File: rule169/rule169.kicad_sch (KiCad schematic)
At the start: 35 parts, among them U1 xiao-ble

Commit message: add project files
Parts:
- added L1, L2, L3: LED, Keyboard Footprints:LED_3mm_reversible, symbol Device:LED
- added R1, R2, R3: 220, Keyboard Footprints:R_1206_DoubleSided, symbol Device:R
- added RSW1: SW_Push, Keyboard Footprints:ResetSW, symbol Switch:SW_Push
- U1: footprint Keyboard Footprints:xiao-ble-tht -> Keyboard Footprints:xiao seed ble
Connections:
- net MCU- is gone; now on net GND: U1.20 (GND)
- net GND: now also R1.2, R2.2, R3.2, RSW1.1
- net MCU+: now also PSW1.1 (A)
- net LED0: now reaches U1.1 (A2/0.02_H)
- net LED0: now also L1.2 (A)
- net RESET: now reaches U1.17 (RESET)
- net RESET: now also RSW1.2
- net LED1: now reaches U1.2 (A4/0.03_H)
- net LED1: now also L2.2 (A)
- net LED2: now reaches U1.3 (A10/0.28)
- net LED2: now also L3.2 (A)
- new net PL1: L1.1 (K), R1.1
- new net PL2: L2.1 (K), R2.1
- new net PL3: L3.1 (K), R3.1
- no-connect marks 11 -> 8
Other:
- note added: "LED"
- note added: "RESET"
- title: (none) -> Automaton 169
- moved on the sheet: BT1, D1, D10, D11, D12, D13, D14, D15, D16, D2, D3, D4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

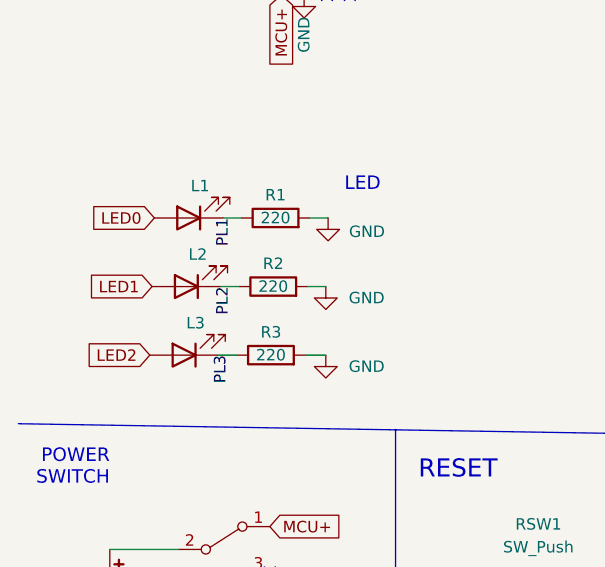
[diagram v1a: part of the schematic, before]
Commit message: add silkscreen
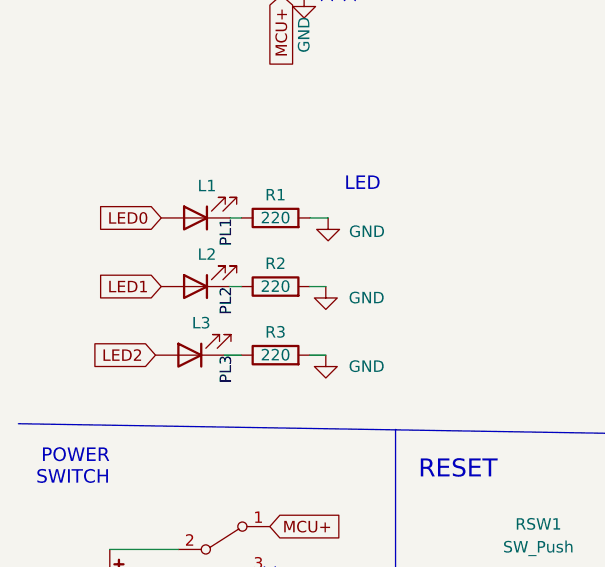
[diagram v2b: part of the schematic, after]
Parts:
- renumbered L2 to L1, L3 to L2, L1 to L3
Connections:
- net LED0: now also L1.2 (A); no longer L3.2 (A)
- net LED1: now also L2.2 (A); no longer L1.2 (A)
- net LED2: now also L3.2 (A); no longer L2.2 (A)
- net PL1: now also L1.1 (K); no longer L3.1 (K)
- net PL2: now also L2.1 (K); no longer L1.1 (K)
- net PL3: now also L3.1 (K); no longer L2.1 (K)
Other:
- moved on the sheet: L1, L2, L3, R3
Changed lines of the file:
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@@
     (stroke (width 0) (type default) (color 0 0 0 0))
   )
-  (wire (pts (xy 36.576 87.63) (xy 34.544 87.63))
+  (wire (pts (xy 35.56 87.63) (xy 36.83 87.63))
+    (stroke (width 0) (type default) (color 0 0 0 0))
+  )
+  (wire (pts (xy 35.56 80.01) (xy 36.83 80.01))
     (stroke (width 0) (type default) (color 0 0 0 0))
   )
@@
     (stroke (width 0) (type default) (color 0 0 0 0))
   )
-  (wire (pts (xy 46.228 95.25) (xy 43.942 95.25))
+  (wire (pts (xy 46.228 95.25) (xy 44.45 95.25))
     (stroke (width 0) (type default) (color 0 0 0 0))
   )
@@
     (stroke (width 0) (type default) (color 0 0 0 0))
   )
+  (wire (pts (xy 34.925 95.25) (xy 36.83 95.25))
+    (stroke (width 0) (type default) (color 0 0 0 0))
+  )
   (wire (pts (xy 142.113 26.162) (xy 142.113 32.512))
     (stroke (width 0) (type default) (color 0 0 0 0))
@@
     (stroke (width 0) (type default) (color 0 0 0 0))
   )
-  (wire (pts (xy 36.83 80.01) (xy 34.798 80.01))
-    (stroke (width 0) (type default) (color 0 0 0 0))
-  )
   (wire (pts (xy 153.035 69.596) (xy 153.035 87.376))
     (stroke (width 0) (type default) (color 0 0 0 0))
@@
     (stroke (width 0) (type default) (color 0 0 0 0))
   )
-  (wire (pts (xy 46.228 87.63) (xy 44.196 87.63))
+  (wire (pts (xy 46.228 87.63) (xy 44.45 87.63))
     (stroke (width 0) (type default) (color 0 0 0 0))
   )
@@
   )
   (wire (pts (xy 169.037 97.536) (xy 179.959 97.536))
-    (stroke (width 0) (type default) (color 0 0 0 0))
-  )
-  (wire (pts (xy 36.322 95.25) (xy 34.29 95.25))
     (stroke (width 0) (type default) (color 0 0 0 0))
   )
@@
     (effects (font (size 1.5 1.5)) (justify right bottom))
   )
-  (label "PL3" (at 35.56 95.25 270)
+  (label "PL3" (at 36.195 95.25 270)
     (effects (font (size 1.27 1.27)) (justify right bottom))
   )
-  (label "PL2" (at 35.814 87.63 270)
+  (label "PL2" (at 36.195 87.63 270)
     (effects (font (size 1.27 1.27)) (justify right bottom))
   )
-  (label "PL1" (at 35.814 80.01 270)
+  (label "PL1" (at 36.195 80.01 270)
     (effects (font (size 1.27 1.27)) (justify right bottom))
   )
@@
     )
   )
-  (global_label "LED1" (shape input) (at 26.924 87.63 180) (fields_autoplaced)
-    (effects (font (size 1.27 1.27)) (justify right))
-    (property "Intersheet References" "${INTERSHEET_REFS}" (id 0) (at 19.8542 87.5506 0)
+  (global_label "LED1" (shape input) (at 27.94 87.63 180) (fields_autoplaced)
+    (effects (font (size 1.27 1.27)) (justify right))
+    (property "Intersheet References" "${INTERSHEET_REFS}" (id 0) (at 20.8702 87.5506 0)
       (effects (font (size 1.27 1.27)) (justify right) hide)
     )
@@
     )
   )
-  (global_label "LED0" (shape input) (at 27.178 80.01 180) (fields_autoplaced)
-    (effects (font (size 1.27 1.27)) (justify right))
-    (property "Intersheet References" "${INTERSHEET_REFS}" (id 0) (at 20.1082 79.9306 0)
-      (effects (font (size 1.27 1.27)) (justify right) hide)
-    )
-  )
-  (global_label "LED2" (shape input) (at 26.67 95.25 180) (fields_autoplaced)
-    (effects (font (size 1.27 1.27)) (justify right))
-    (property "Intersheet References" "${INTERSHEET_REFS}" (id 0) (at 19.6002 95.1706 0)
+  (global_label "LED0" (shape input) (at 27.94 80.01 180) (fields_autoplaced)
+    (effects (font (size 1.27 1.27)) (justify right))
+    (property "Intersheet References" "${INTERSHEET_REFS}" (id 0) (at 20.8702 79.9306 0)
+      (effects (font (size 1.27 1.27)) (justify right) hide)
+    )
+  )
+  (global_label "LED2" (shape input) (at 27.305 95.25 180) (fields_autoplaced)
+    (effects (font (size 1.27 1.27)) (justify right))
+    (property "Intersheet References" "${INTERSHEET_REFS}" (id 0) (at 20.2352 95.1706 0)
       (effects (font (size 1.27 1.27)) (justify right) hide)
     )
@@
     (pin "2")
   )
-  (symbol (lib_id "Device:LED") (at 30.734 87.63 180) (unit 1)
-    (in_bom yes) (on_board yes)
-    (property "Reference" "L2" (id 0) (at 32.004 84.074 0))
-    (property "Value" "LED" (id 1) (at 32.3215 82.296 0)
-      (effects (font (size 1.27 1.27)) hide)
-    )
-    (property "Footprint" "Keyboard Footprints:LED_3mm_reversible" (id 2) (at 30.734 87.63 0)
-      (effects (font (size 1.27 1.27)) hide)
-    )
-    (property "Datasheet" "~" (id 3) (at 30.734 87.63 0)
+  (symbol (lib_id "Device:LED") (at 31.75 80.01 180) (unit 1)
+    (in_bom yes) (on_board yes)
+    (property "Reference" "L1" (id 0) (at 33.02 76.454 0))
+    (property "Value" "LED" (id 1) (at 33.3375 74.676 0)
+      (effects (font (size 1.27 1.27)) hide)
+    )
+    (property "Footprint" "Keyboard Footprints:LED_3mm_reversible" (id 2) (at 31.75 80.01 0)
+      (effects (font (size 1.27 1.27)) hide)
+    )
+    (property "Datasheet" "~" (id 3) (at 31.75 80.01 0)
       (effects (font (size 1.27 1.27)) hide)
     )
@@
     (pin "1")
   )
-  (symbol (lib_id "Device:R") (at 40.132 95.25 90) (unit 1)
-    (in_bom yes) (on_board yes)
-    (property "Reference" "R3" (id 0) (at 40.132 92.71 90))
-    (property "Value" "220" (id 1) (at 40.132 95.25 90))
-    (property "Footprint" "Keyboard Footprints:R_1206_DoubleSided" (id 2) (at 40.132 97.028 90)
-      (effects (font (size 1.27 1.27)) hide)
-    )
-    (property "Datasheet" "~" (id 3) (at 40.132 95.25 0)
+  (symbol (lib_id "Device:R") (at 40.64 95.25 90) (unit 1)
+    (in_bom yes) (on_board yes)
+    (property "Reference" "R3" (id 0) (at 40.64 92.71 90))
+    (property "Value" "220" (id 1) (at 40.64 95.25 90))
+    (property "Footprint" "Keyboard Footprints:R_1206_DoubleSided" (id 2) (at 40.64 97.028 90)
+      (effects (font (size 1.27 1.27)) hide)
+    )
+    (property "Datasheet" "~" (id 3) (at 40.64 95.25 0)
       (effects (font (size 1.27 1.27)) hide)
     )
@@
     (pin "1")
   )
-  (symbol (lib_id "Device:LED") (at 30.48 95.25 180) (unit 1)
-    (in_bom yes) (on_board yes)
-    (property "Reference" "L3" (id 0) (at 31.75 91.694 0))
-    (property "Value" "LED" (id 1) (at 32.0675 89.916 0)
-      (effects (font (size 1.27 1.27)) hide)
-    )
-    (property "Footprint" "Keyboard Footprints:LED_3mm_reversible" (id 2) (at 30.48 95.25 0)
-      (effects (font (size 1.27 1.27)) hide)
-    )
-    (property "Datasheet" "~" (id 3) (at 30.48 95.25 0)
+  (symbol (lib_id "Device:LED") (at 31.75 87.63 180) (unit 1)
+    (in_bom yes) (on_board yes)
+    (property "Reference" "L2" (id 0) (at 33.02 84.074 0))
+    (property "Value" "LED" (id 1) (at 33.3375 82.296 0)
+      (effects (font (size 1.27 1.27)) hide)
+    )
+    (property "Footprint" "Keyboard Footprints:LED_3mm_reversible" (id 2) (at 31.75 87.63 0)
+      (effects (font (size 1.27 1.27)) hide)
+    )
+    (property "Datasheet" "~" (id 3) (at 31.75 87.63 0)
       (effects (font (size 1.27 1.27)) hide)
     )
@@
     (pin "2")
   )
-  (symbol (lib_id "Device:R") (at 40.386 87.63 90) (unit 1)
-    (in_bom yes) (on_board yes)
-    (property "Reference" "R2" (id 0) (at 40.386 85.09 90))
-    (property "Value" "220" (id 1) (at 40.386 87.63 90))
-    (property "Footprint" "Keyboard Footprints:R_1206_DoubleSided" (id 2) (at 40.386 89.408 90)
-      (effects (font (size 1.27 1.27)) hide)
-    )
-    (property "Datasheet" "~" (id 3) (at 40.386 87.63 0)
+  (symbol (lib_id "Device:R") (at 40.64 87.63 90) (unit 1)
+    (in_bom yes) (on_board yes)
+    (property "Reference" "R2" (id 0) (at 40.64 85.09 90))
+    (property "Value" "220" (id 1) (at 40.64 87.63 90))
+    (property "Footprint" "Keyboard Footprints:R_1206_DoubleSided" (id 2) (at 40.64 89.408 90)
+      (effects (font (size 1.27 1.27)) hide)
+    )
+    (property "Datasheet" "~" (id 3) (at 40.64 87.63 0)
       (effects (font (size 1.27 1.27)) hide)
     )
@@
     (pin "2")
   )
-  (symbol (lib_id "Device:LED") (at 30.988 80.01 180) (unit 1)
-    (in_bom yes) (on_board yes)
-    (property "Reference" "L1" (id 0) (at 32.258 76.454 0))
-    (property "Value" "LED" (id 1) (at 32.5755 74.676 0)
-      (effects (font (size 1.27 1.27)) hide)
-    )
-    (property "Footprint" "Keyboard Footprints:LED_3mm_reversible" (id 2) (at 30.988 80.01 0)
-      (effects (font (size 1.27 1.27)) hide)
-    )
-    (property "Datasheet" "~" (id 3) (at 30.988 80.01 0)
+  (symbol (lib_id "Device:LED") (at 31.115 95.25 180) (unit 1)
+    (in_bom yes) (on_board yes)
+    (property "Reference" "L3" (id 0) (at 32.385 91.694 0))
+    (property "Value" "LED" (id 1) (at 32.7025 89.916 0)
+      (effects (font (size 1.27 1.27)) hide)
+    )
+    (property "Footprint" "Keyboard Footprints:LED_3mm_reversible" (id 2) (at 31.115 95.25 0)
+      (effects (font (size 1.27 1.27)) hide)
+    )
+    (property "Datasheet" "~" (id 3) (at 31.115 95.25 0)
       (effects (font (size 1.27 1.27)) hide)
     )
@@
       (reference "D16") (unit 1) (value "D_Small") (footprint "Keyboard Footprints:Diode_SOD123")
     )
+    (path "/2965f5f3-e9ab-46d6-8907-ca3e807ed128"
+      (reference "L1") (unit 1) (value "LED") (footprint "Keyboard Footprints:LED_3mm_reversible")
+    )
+    (path "/6867fbb1-6ae8-4277-96c6-9754739e207e"
+      (reference "L2") (unit 1) (value "LED") (footprint "Keyboard Footprints:LED_3mm_reversible")
+    )
     (path "/d6401ad6-f848-4cc0-b47a-df0b179d6b71"
-      (reference "L1") (unit 1) (value "LED") (footprint "Keyboard Footprints:LED_3mm_reversible")
-    )
-    (path "/2965f5f3-e9ab-46d6-8907-ca3e807ed128"
-      (reference "L2") (unit 1) (value "LED") (footprint "Keyboard Footprints:LED_3mm_reversible")
-    )
-    (path "/6867fbb1-6ae8-4277-96c6-9754739e207e"
       (reference "L3") (unit 1) (value "LED") (footprint "Keyboard Footprints:LED_3mm_reversible")
     )
